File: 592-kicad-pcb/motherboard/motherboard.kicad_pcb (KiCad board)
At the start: 4 copper layers, 202 parts, among them J1 U.FL, J10 Conn_02x06_Odd_Even, J11 Conn_02x06_Odd_Even, J12 Conn_02x06_Odd_Even, J13 Conn_02x06_Odd_Even, J14 Conn_02x06_Odd_Even, J15 Conn_02x06_Odd_Even, J16 Conn_02x06_Odd_Even, J17 Conn_02x06_Odd_Even, J18 USB_B_Micro, J19 Micro_SD_Card, J2 U.FL, J20 Conn_02x01, J21 Conn_02x01, J22 Conn_02x01, J23 Conn_02x01, J24 Conn_02x01, J25 Conn_02x01, J26 Conn_02x01, J3 DF40C-40DP-0.4V(51), J31 Conn_02x01, J4 DF40C-40DP-0.4V(51), J8 2.54mm jumper, J9 U.FL, SW1 C318884, U1 NUCLEO144-H743ZI, U10 SN74LVC1G3157DBVR, U11 FT4232H, U12 74HC595, U13 W25Q32JVSS, U14 SN74LVC1G3157DBVR, U15 SN74LVC1G14DBV, U16 SN74LVC1G00DCK, U17 74CBTLV3257PW,118, U18 SN74LVC1G14DBV, U19 74CBTLV3257PW,118, U2 OPA2328DGKR, U20 74CBTLV3257PW,118, U21 74CBTLV3257PW,118, U29 74CBTLV3257PW,118, U3 74LVC1T45GW, U30 74CBTLV3257PW,118, U31 74CBTLV3257PW,118, U32 74CBTLV3257PW,118, U4 SN74LVC1G14DBV, U5 74LVC1T45GW, U6 SMXS-04K, U7 SX3M10.000B10F20TNN, U8 74LVC1T45GW, U9 SN74LVC1G3157DBVR, Y1 NX3225GA-25.000M-STD-CRG-2, Y2 Si5351A, Y3 X322512MSB4SI

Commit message: add FTDI local routing, muxes
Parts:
- removed R4: 10M, Resistor_SMD:R_0603_1608Metric
- moved R12 297.0 mm to (189.4, 77.9), turned to 180 degrees
- moved R13 282.9 mm to (185.5, 79.5)
- moved R5 258.2 mm to (158.9, 102.7)
- moved R3 255.2 mm to (160.2, 101.2), turned to 180 degrees
- moved R6 255.1 mm to (157.9, 88.8), turned to -90 degrees
- moved R7 253.6 mm to (156.4, 88.8), turned to -90 degrees
- moved R11 246.0 mm to (189.4, 79.4)
- moved R2 243.7 mm to (140.9, 106.8), turned to -90 degrees
- moved R36 203.7 mm to (118.8, 95.9)
- moved R35 203.6 mm to (120.0, 95.9)
- moved R38 201.1 mm to (117.2, 96.5), turned to 180 degrees
- moved C20 200.3 mm to (117.2, 95.2), turned to 180 degrees
- moved C14 199.2 mm to (117.2, 99.5), turned to 0 degrees
- moved C53 199.2 mm to (-96.8, 140.6), turned to 180 degrees
- moved C18 194.8 mm to (115.6, 96.7), turned to 90 degrees
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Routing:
- net /motherboard_top/chip_rck_jtag_tdi: track 1.45 -> 43.4 mm, vias 1 -> 2
- net /motherboard_top/chip_rck_jtag_tms: track 1.59 -> 42.4 mm, vias 1 -> 2
- net /motherboard_top/chip_rck_jtag_tck: track 3.67 -> 36.3 mm, vias 1 -> 4
- net +3V3: track 12.2 -> 43.1 mm
- net /motherboard_top/chip_rck_jtag_tdo: track 0.78 -> 30.1 mm, vias 1 -> 4
- net /motherboard_top/GPIO_JTAG_FTDI_source_select: track 0.00 -> 19.0 mm, vias 0 -> 1
- net /motherboard_top/mgmt_sdi: track 1.51 -> 14.4 mm, vias 1 -> 2
- net /motherboard_top/mgmt_sck: track 1.57 -> 12.2 mm, vias 1 -> 2
- net /motherboard_top/mgmt_csb: track 1.35 -> 11.7 mm, vias 1 -> 2
- net /motherboard_top/chip_rck_i2c_sda: track 2.15 -> 11.2 mm, vias 1 -> 0
- net /motherboard_top/mgmt_sdo: track 1.61 -> 10.3 mm, vias 1 -> 2
- net VBUS: track 0.00 -> 7.38 mm
- net /motherboard_top/ftdi/ftdi_1v8: track 0.00 -> 7.01 mm
- net /motherboard_top/chip_nfc_jtag_tdi: track 33.6 -> 40.6 mm
- net Net-(U11-OSCO): track 0.00 -> 6.59 mm
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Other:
- board text removed: "bogos binted?"

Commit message: further routing progess: core routing done
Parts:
- added R15: 5k, Resistor_SMD:R_0402_1005Metric, F.Cu at (160.6, 92.5)
- added R4: 5k, Resistor_SMD:R_0402_1005Metric, F.Cu at (159.8, 94.7)
- R68, R69: value 2k -> 5k
- moved J8 286.3 mm to (194.8, 114.2), turned to -90 degrees
- moved R22 264.3 mm to (174.1, 107.3), turned to 180 degrees
- moved C53 249.2 mm to (150.8, 113.2)
- moved R19 248.9 mm to (150.8, 114.3)
- moved SW1 184.7 mm to (198.3, 109.5), turned to 0 degrees
- moved R21 177.5 mm to (192.3, 107.6)
- moved C3 177.3 mm to (193.9, 109.7), turned to -90 degrees
- moved U4 176.8 mm to (191.8, 109.5), turned to 180 degrees
- moved U5 176.1 mm to (188.4, 108.2), turned to 0 degrees
- moved U14 153.3 mm to (183.2, 85.8), turned to 180 degrees
- moved C35 153.1 mm to (181.6, 88.3), turned to -90 degrees
- moved J19 148.8 mm to (198.0, 87.6), turned to 90 degrees
- moved C33 146.9 mm to (187.7, 83.7), turned to 0 degrees
- moved R50 146.9 mm to (181.6, 90.3), turned to 90 degrees
- moved U13 146.2 mm to (185.3, 92.9), turned to -90 degrees
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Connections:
- J19 pad 11: (no net) -> Net-(J19-SHIELD)
- J19 pad 9: Net-(J19-SHIELD) -> (no net)
- U17 pad 10: unconnected-(U17-Pad10) -> /motherboard_top/chip_spi_flash_0_sck
- U17 pad 11: unconnected-(U17-Pad11) -> /motherboard_top/ftdi_spi_sck
- U17 pad 12: unconnected-(U17-Pad12) -> /motherboard_top/rck_mem_cs
- U17 pad 13: unconnected-(U17-Pad13) -> /motherboard_top/chip_spi_flash_0_cs_0
- U17 pad 14: unconnected-(U17-Pad14) -> /motherboard_top/ftdi_spi_cs
- U17 pad 2: Net-(R57-Pad2) -> unconnected-(U17-Pad2)
- U17 pad 3: /motherboard_top/chip_spi_flash_0_dq_3 -> unconnected-(U17-Pad3)
- U17 pad 4: /motherboard_top/rck_mem_io3 -> unconnected-(U17-Pad4)
- U17 pad 5: Net-(R58-Pad2) -> unconnected-(U17-Pad5)
- U17 pad 6: /motherboard_top/chip_spi_flash_0_dq_2 -> unconnected-(U17-Pad6)
- U17 pad 7: /motherboard_top/rck_mem_io2 -> unconnected-(U17-Pad7)
- U17 pad 9: unconnected-(U17-Pad9) -> /motherboard_top/rck_mem_sck
- U20 pad 10: /motherboard_top/chip_spi_flash_0_dq_1 -> /motherboard_top/chip_spi_flash_0_dq_0
- U20 pad 11: /motherboard_top/ftdi_spi_miso -> /motherboard_top/ftdi_spi_mosi
- U20 pad 12: /motherboard_top/rck_mem_sck -> /motherboard_top/rck_mem_miso_i01
- U20 pad 13: /motherboard_top/chip_spi_flash_0_sck -> /motherboard_top/chip_spi_flash_0_dq_1
- U20 pad 14: /motherboard_top/ftdi_spi_sck -> /motherboard_top/ftdi_spi_miso
- U20 pad 2: /motherboard_top/ftdi_spi_mosi -> Net-(R58-Pad2)
- U20 pad 3: /motherboard_top/chip_spi_flash_0_dq_0 -> /motherboard_top/chip_spi_flash_0_dq_2
- U20 pad 4: /motherboard_top/rck_mem_mosi_io0 -> /motherboard_top/rck_mem_io2
- U20 pad 5: /motherboard_top/ftdi_spi_cs -> Net-(R57-Pad2)
- U20 pad 6: /motherboard_top/chip_spi_flash_0_cs_0 -> /motherboard_top/chip_spi_flash_0_dq_3
- U20 pad 7: /motherboard_top/rck_mem_cs -> /motherboard_top/rck_mem_io3
- U20 pad 9: /motherboard_top/rck_mem_miso_i01 -> /motherboard_top/rck_mem_mosi_io0
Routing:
- net /motherboard_top/rck_mem_miso_i01: track 0.00 -> 49.3 mm, vias 0 -> 3
- net /motherboard_top/ftdi_spi_cs: track 4.15 -> 53.4 mm, vias 1 -> 4
- net /motherboard_top/ftdi_spi_miso: track 3.80 -> 51.5 mm, vias 1 -> 3
- net /motherboard_top/ftdi_spi_sck: track 1.49 -> 48.9 mm, vias 1 -> 2
- net /motherboard_top/spi_mgmt_enb: track 0.00 -> 46.3 mm, vias 0 -> 2
- net /motherboard_top/rck_mem_mosi_io0: track 0.00 -> 43.9 mm, vias 0 -> 2
- net /motherboard_top/ftdi_spi_mosi: track 2.15 -> 44.5 mm, vias 1 -> 3
- net /motherboard_top/rck_mem_sck: track 0.00 -> 34.6 mm, vias 0 -> 3
- net /motherboard_top/chip_nfc_jtag_trst: track 2.21 -> 31.5 mm, vias 1 -> 2
- net /motherboard_top/chip_spi_flash_0_dq_0: track 0.95 -> 29.5 mm, vias 1 -> 2
- net /motherboard_top/chip_spi_flash_0_dq_1: track 0.88 -> 26.9 mm, vias 1 -> 2
- net /motherboard_top/rck_mem_io3: track 0.00 -> 25.8 mm, vias 0 -> 2
- net /motherboard_top/GPIO_rck_mem_source_sel_ftdiB: track 0.00 -> 22.8 mm, vias 0 -> 2
- net /motherboard_top/chip_nfc_vref: track 1.98 -> 24.1 mm
- net /motherboard_top/chip_spi_flash_0_sck: track 2.09 -> 22.2 mm, vias 1 -> 2
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
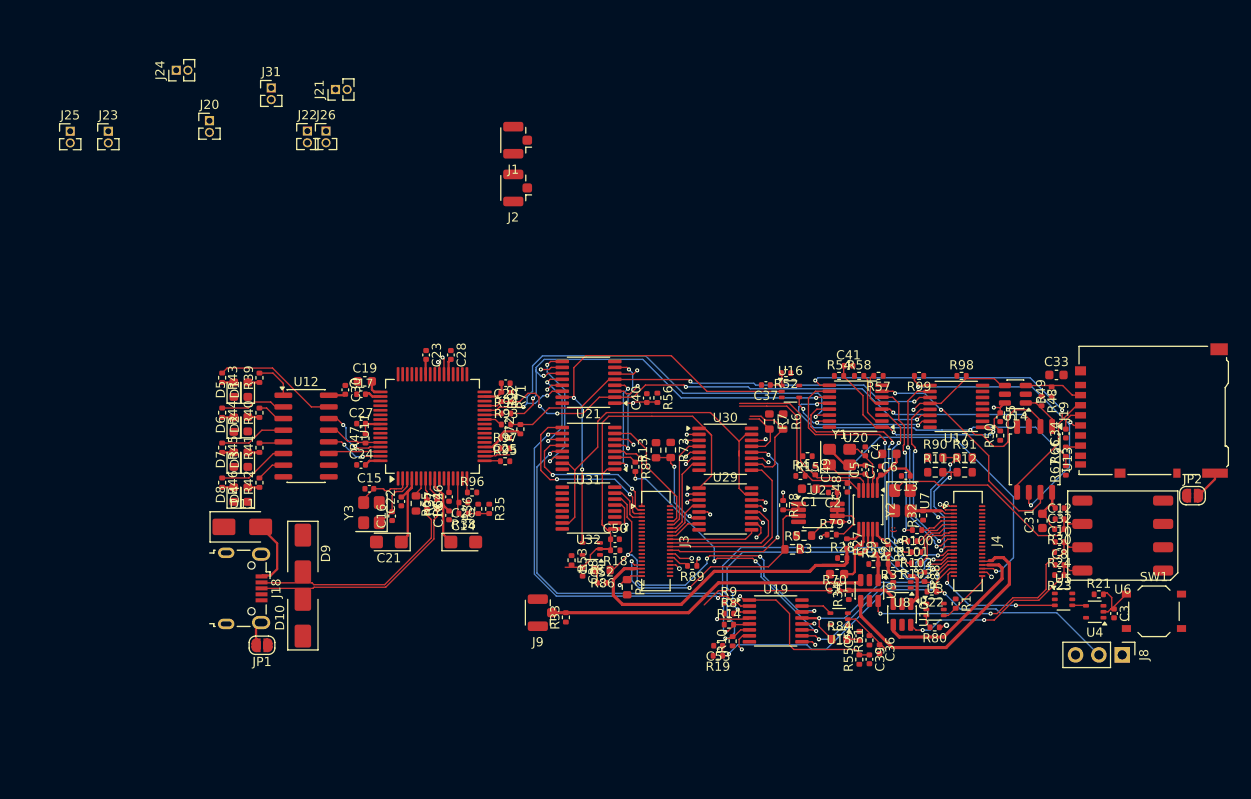
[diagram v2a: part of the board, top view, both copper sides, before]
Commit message: complete routing for core
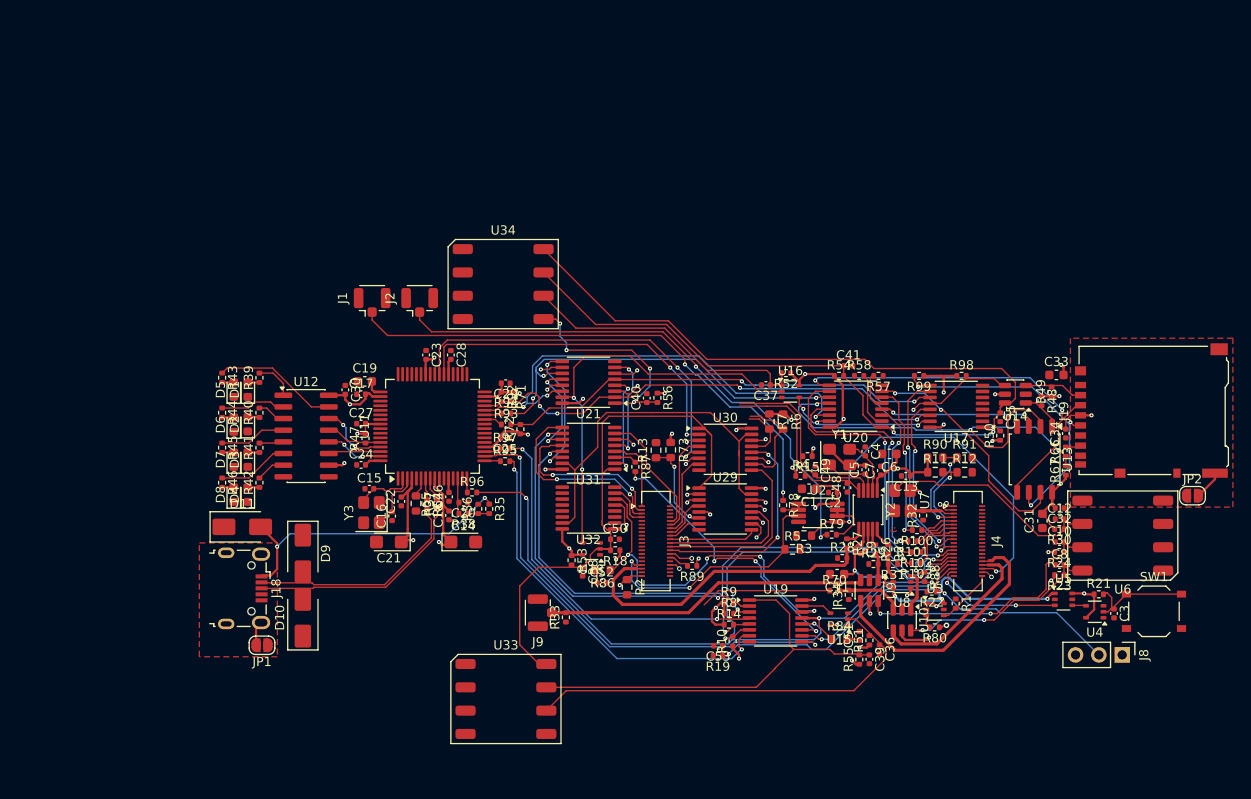
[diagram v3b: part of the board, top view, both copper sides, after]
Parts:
- removed J20, J21, J22, J23, J24, J25, J26, J31: Conn_02x01, Connector_PinHeader_1.27mm:PinHeader_1x02_P1.27mm_Vertical
- added U33: SMXS-04K, 592-partslib:SMXS-04K-TP, F.Cu at (127.7, 119.0)
- added U34: SMXS-04K, 592-partslib:SMXS-04K-TP, F.Cu at (127.4, 73.8)
- moved J1 23.7 mm to (113.1, 75.8), turned to 90 degrees
- moved J2 16.4 mm to (118.3, 75.8), turned to 90 degrees
- moved U10 0.61 mm to (170.8, 110.4)
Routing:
- net +3V3: track 55.5 -> 151.5 mm, vias 0 -> 45
- net /motherboard_top/GPIO_rck_mem_sel_sdB: track 5.22 -> 65.0 mm, vias 1 -> 0
- net /motherboard_top/ADC_chip_ana_mux_out_2: track 0.80 -> 59.6 mm, vias 1 -> 2
- net /motherboard_top/ADC_chip_ana_mux_out_1: track 0.88 -> 58.0 mm, vias 1 -> 2
- net /motherboard_top/ftdi1_jtag_tck: track 1.37 -> 51.4 mm, vias 1 -> 2
- net /motherboard_top/ftdi1_jtag_tdo: track 4.37 -> 53.0 mm, vias 1 -> 2
- net /motherboard_top/ftdi1_jtag_tdi: track 2.50 -> 43.1 mm, vias 1 -> 2
- net /motherboard_top/GPIO_ftdi_jtag_src_en: track 5.52 -> 45.9 mm
- net /PE0_UART8_RX: track 3.02 -> 42.6 mm
- net /motherboard_top/GPIO_rck_mem_source_sel_ftdiB: track 22.8 -> 59.8 mm
- net /motherboard_top/ftdi1_jtag_tms: track 3.58 -> 40.3 mm, vias 1 -> 2
- net /PE1_UART8_TX: track 3.23 -> 38.2 mm
- net /motherboard_top/GPIO_rck_mem_source_en: track 2.64 -> 32.1 mm
- net +1V8: track 6.48 -> 34.7 mm, vias 0 -> 5
- net /motherboard_top/GPIO_JTAG_FTDI_source_select: track 19.0 -> 47.1 mm, vias 1 -> 0
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- added copper zone on In2.Cu, net +3V3
- added copper zone on In1.Cu, net GND
- added copper zone on F.Cu, net Net-(J18-Shield)
- added copper zone on F.Cu, net Net-(J19-SHIELD)

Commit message: halfway done routing to edge, next is analog header, gnd
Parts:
- removed JP3, JP4, JP5: SolderJumper_2_Bridged, Jumper:SolderJumper-2_P1.3mm_Bridged2Bar_Pad1.0x1.5mm
- moved J10 299.9 mm to (179.2, 135.0), turned to 90 degrees
- moved J11 293.1 mm to (191.2, 60.5), turned to -90 degrees
- moved U1 279.3 mm to (184.8, 66.1), turned to -90 degrees
- moved J13 272.7 mm to (170.2, 60.5), turned to -90 degrees
- moved J14 259.4 mm to (157.8, 135.0), turned to 90 degrees
- moved J16 253.9 mm to (149.2, 60.5), turned to -90 degrees
- moved J17 238.8 mm to (136.5, 135.0), turned to 90 degrees
- moved J12 229.6 mm to (128.0, 60.5), turned to -90 degrees
- moved R68 220.9 mm to (183.1, 124.8), turned to 180 degrees
- moved J15 217.7 mm to (115.5, 135.0), turned to 90 degrees
- moved R69 216.1 mm to (179.0, 124.8)
- moved J2 88.4 mm to (194.6, 120.4), turned to -90 degrees
- moved J1 88.1 mm to (189.1, 120.4), turned to -90 degrees
- moved U34 16.8 mm to (110.9, 77.0)
- moved J8 5.08 mm to (189.8, 114.2), turned to 90 degrees
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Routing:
- net /PE0_UART8_RX: track 42.6 -> 128.6 mm, vias 2 -> 3
- net /PG12: track 3.12 -> 85.9 mm, vias 1 -> 3
- net /motherboard_top/ADC_chip_ana_mux_out_2: track 59.6 -> 0.00 mm, vias 2 -> 0
- net /motherboard_top/chip_rck_jtag_tck: track 39.7 -> 93.6 mm, vias 4 -> 5
- net /motherboard_top/chip_rck_jtag_tdo: track 30.7 -> 84.6 mm, vias 4 -> 5
- net /motherboard_top/chip_nfc_jtag_tdi: track 40.6 -> 93.1 mm, vias 2 -> 3
- net /motherboard_top/GPIO_chip_rck_reset_io: track 10.1 -> 60.3 mm, vias 2 -> 4
- net /motherboard_top/chip_rck_jtag_tms: track 41.3 -> 91.4 mm
- net /motherboard_top/chip_rck_jtag_tdi: track 42.1 -> 92.0 mm
- net /motherboard_top/chip_rck_gpio_1_0: track 1.61 -> 47.5 mm, vias 1 -> 3
- net /motherboard_top/GPIO_chip_nfc_jtag_tdo2: track 0.88 -> 46.4 mm, vias 1 -> 5
- net /motherboard_top/chip_rck_spi_0_sck: track 1.40 -> 42.8 mm, vias 1 -> 3
- net /motherboard_top/chip_rck_gpio_0_0: track 2.46 -> 43.5 mm, vias 1 -> 3
- net /PE1_UART8_TX: track 38.2 -> 76.8 mm, vias 2 -> 4
- net /motherboard_top/chip_rck_i2c_scl: track 6.29 -> 44.6 mm, vias 0 -> 2
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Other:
- board outline added: 125 x 85 mm
